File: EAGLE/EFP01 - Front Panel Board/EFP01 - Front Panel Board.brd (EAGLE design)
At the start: 200 x 65 mm, 151 parts, among them J1 PWRBTN, J16 S8B-PH-SM4, J17 S8B-PH-SM4, J18 S6B-PH-SM4, J2 ESTOP, J20 Intel EDISON, J3 USB-A(2.0), J5 LCD, J6 S8B-PH-SM4, J7 USB-B, Q2 25MHz, U1 74LVC1T45, U10 FT231XS-R, U11 74LVC1T45, U12 74LVC1T45, U13 74LVC1T45, U14 74LVC1T45, U15 74LVC1T45, U17 OR, U18 MIC2026-1YM, U19 MIC2026-1YM, U2 74LVC1T45, U20 OR, U21 74LVC1T45, U22 74LVC1T45, U23 74LVC1T45, U24 74LVC1T45, U25 74LVC1T45, U26 74LVC1T45, U27 74LVC1T45, U28 74LVC1T45, U3 93LC66A, U30 74LVC1T45, U4 LAN9514, U5 74LVC1T45, U6 74LVC1T45, U7 74LVC1T45, U8 74LVC1T45, U9 SP3485

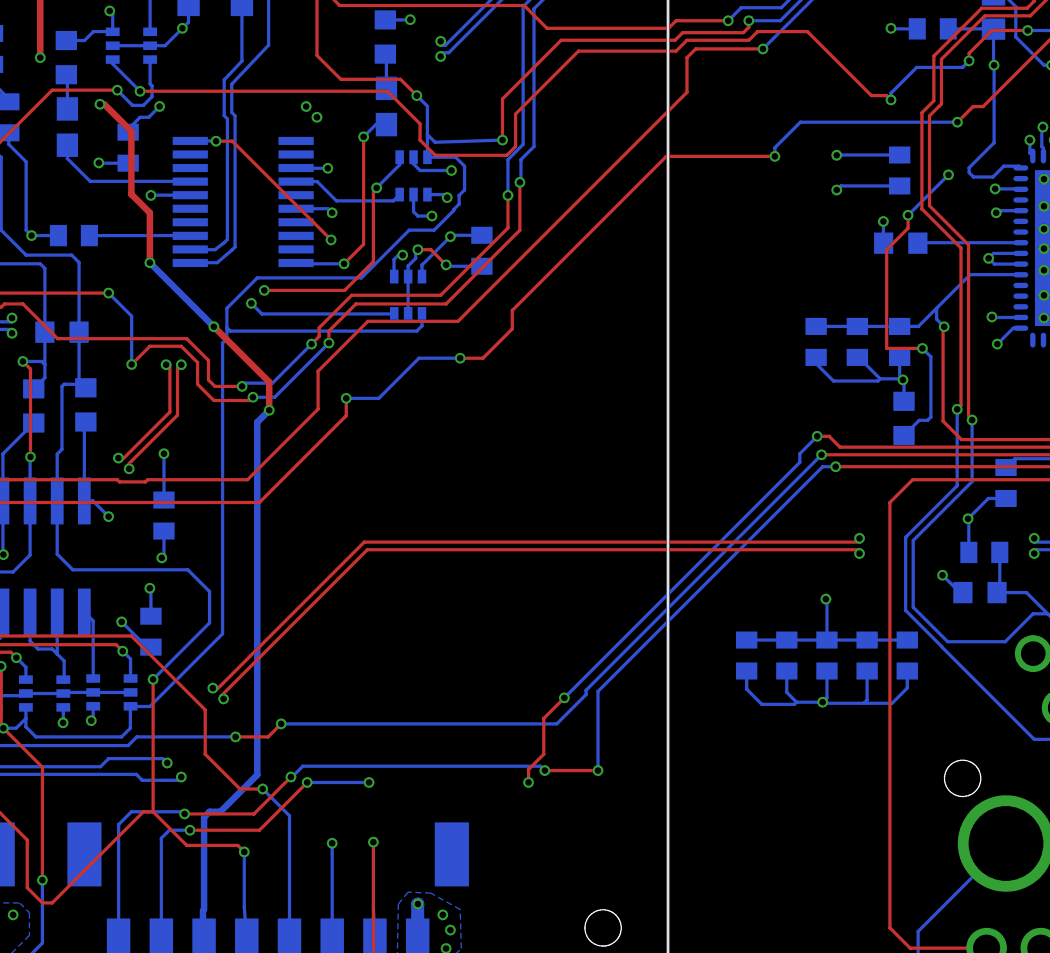
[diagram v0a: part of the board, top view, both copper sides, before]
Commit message: Fixed BOM, began adding DFM changes
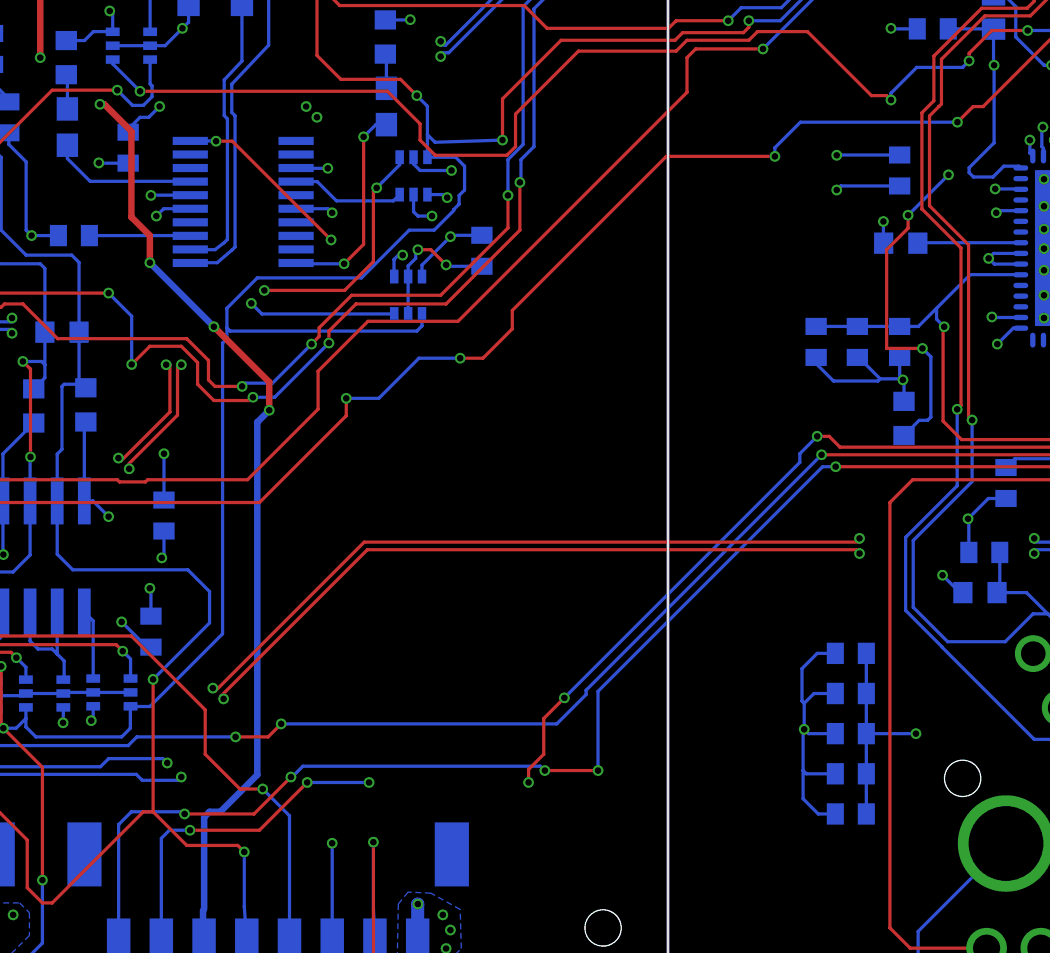
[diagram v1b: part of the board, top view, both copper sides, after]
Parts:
- moved C23 7.87 mm to (154.4, 12.4), turned to 180 degrees
- moved C79 5.59 mm to (154.4, 14.3), turned to 180 degrees
- moved C82 4.88 mm to (154.4, 20.0), turned to 180 degrees
- moved C80 3.82 mm to (154.4, 16.2), turned to 180 degrees
- moved C81 3.48 mm to (154.4, 18.1), turned to 180 degrees
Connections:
- net +3V3: now also U10.15
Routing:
- net +3V3: track 217.1 -> 219.2 mm, vias 60 -> 61

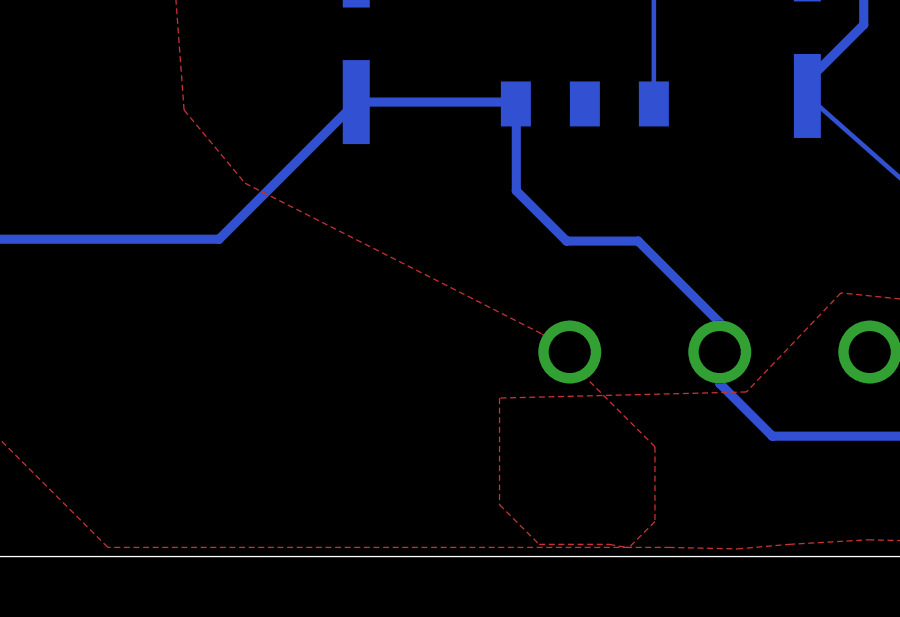
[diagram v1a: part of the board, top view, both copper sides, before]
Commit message: Made REV 2 modifications, including increasing width of power traces, adding vias to power traces, and addition of LEDs to all modular tools. Catch diodes added to ESOL01 board to prevent coils from creating problems "upstream"
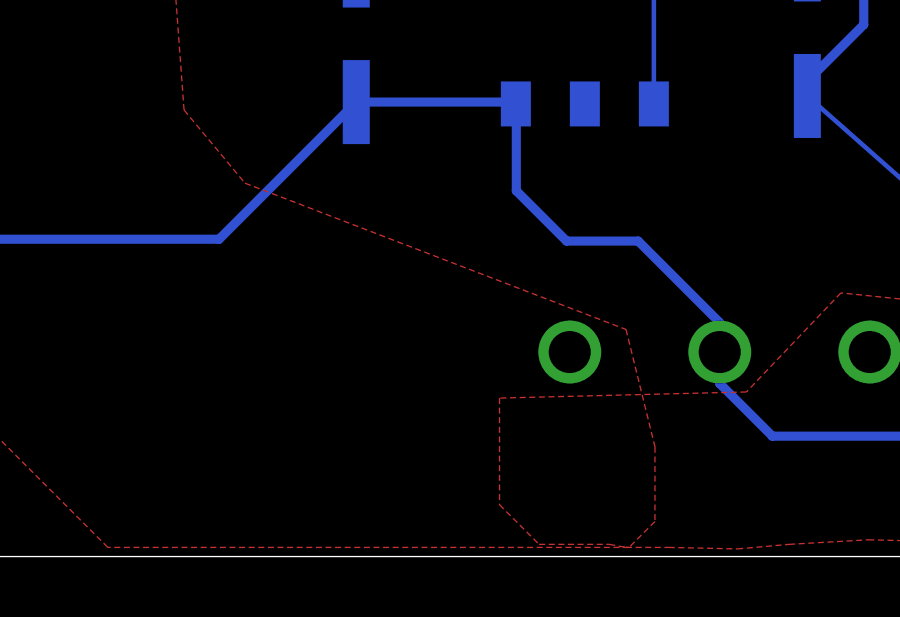
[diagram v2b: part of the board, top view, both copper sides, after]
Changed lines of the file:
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@@
 <polygon width="0" layer="1" thermals="no">
 <vertex x="21.1836" y="12.446"/>
-<vertex x="31.0896" y="7.4168"/>
+<vertex x="33.8836" y="7.5692"/>
 <vertex x="34.8488" y="3.6576"/>
 <vertex x="34.8488" y="1.1684"/>

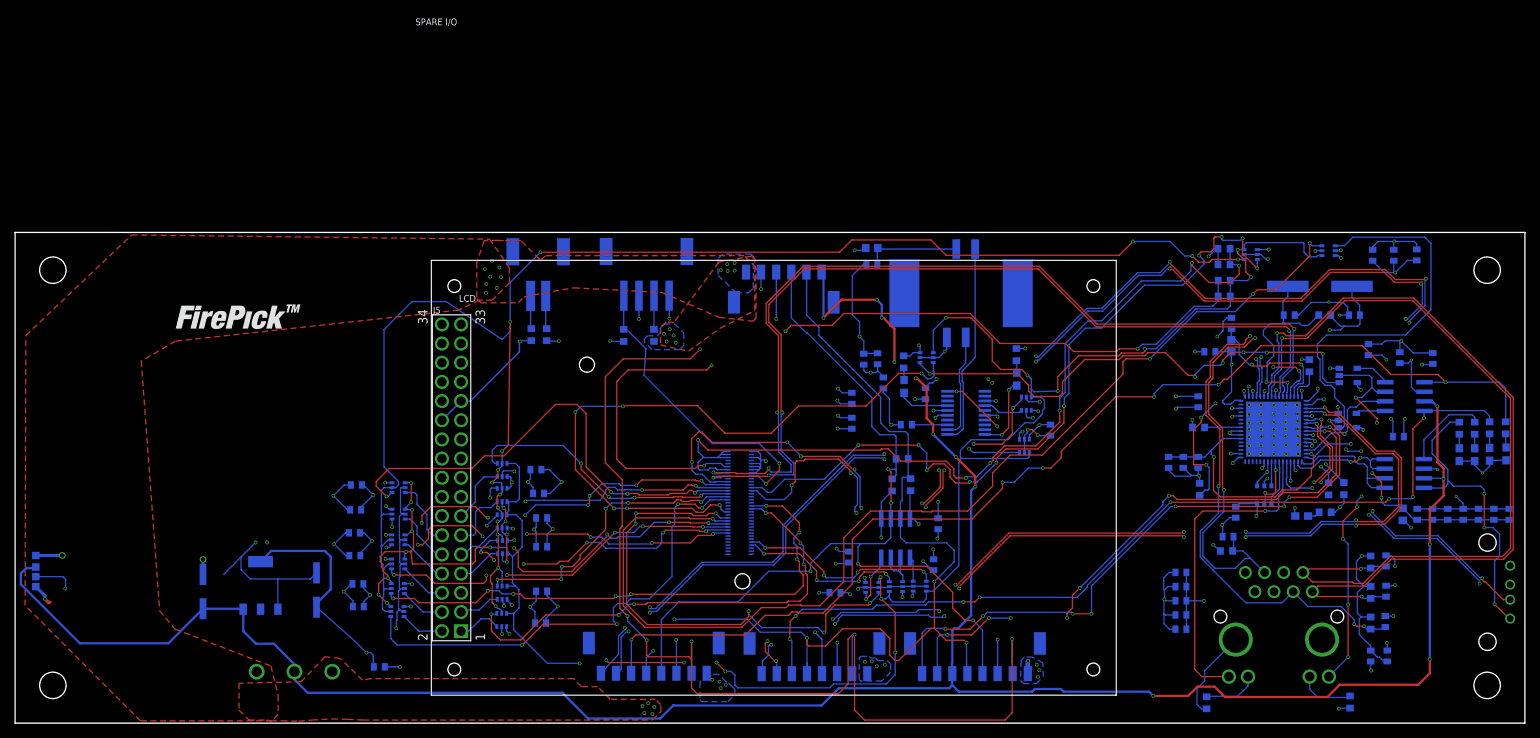
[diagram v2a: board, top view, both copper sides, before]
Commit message: Routing for differential pairs included in EFP01. Minor changes to BOM, inventory list.
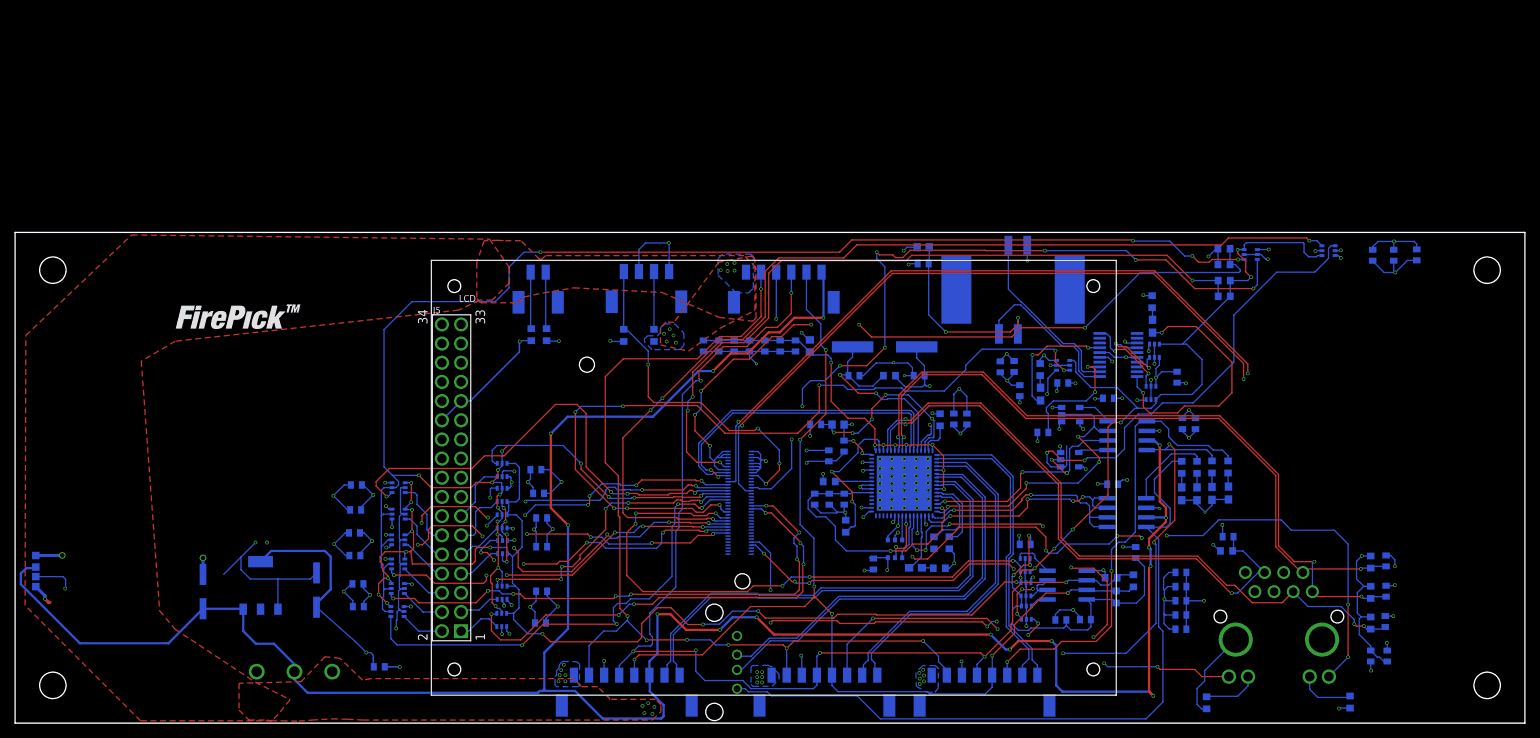
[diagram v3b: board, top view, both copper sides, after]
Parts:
- J1: device TinWhiskers:CON-JST-PH-2.0MM-4P-SMT-RA -> TinWhiskers:CON-JST-PH-2.0MM-4P-SMT-VRT
- J2: device TinWhiskers:CON-JST-PH-2.0MM-2P-SMT-RA -> TinWhiskers:CON-JST-PH-2.0MM-2P-SMT-VRT
- moved C22 109.0 mm to (91.2, 50.0), turned to 90 degrees
- moved C21 105.1 mm to (93.2, 50.0), turned to 90 degrees
- moved J3 102.8 mm to (92.6, 8.05)
- moved C20 101.1 mm to (95.2, 50.0), turned to 90 degrees
- moved C19 97.1 mm to (97.3, 50.0), turned to 90 degrees
- moved C18 93.2 mm to (99.3, 50.0), turned to 90 degrees
- moved C14 89.2 mm to (101.3, 50.0), turned to 90 degrees
- moved C13 85.3 mm to (103.4, 50.0), turned to 90 degrees
- moved FB1 81.6 mm to (105.3, 50.0), turned to 90 degrees
- moved C12 58.2 mm to (119.8, 46.0)
- moved Q2 58.2 mm to (115.2, 49.8)
- moved R11 58.2 mm to (115.8, 46.0)
- moved C11 58.2 mm to (111.1, 46.0)
- moved C73 56.7 mm to (106.0, 39.6), turned to 180 degrees
- moved FB4 53.1 mm to (109.0, 39.5), turned to 180 degrees
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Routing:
- net ULC_N: track 171.6 -> 39.4 mm, vias 9 -> 0
- net ULC_P: track 167.0 -> 38.8 mm, vias 9 -> 0
- net PWR2: track 150.7 -> 61.5 mm, vias 6 -> 2
- net USB0_P: track 122.3 -> 42.9 mm, vias 4 -> 0
- net USB0_N: track 120.8 -> 41.4 mm, vias 4 -> 2
- net EE_N: track 121.0 -> 45.6 mm, vias 8 -> 0
- net EE_P: track 120.4 -> 45.0 mm, vias 9 -> 0
- net PWR3: track 39.8 -> 97.8 mm, vias 3 -> 0
- net ULCENO: track 67.9 -> 10.3 mm, vias 6 -> 2
- net SCED_P: track 53.9 -> 108.7 mm, vias 6 -> 3
- net LED_TXRX: track 39.9 -> 89.7 mm, vias 6 -> 8
- net !ENBL_MOD: track 167.1 -> 124.3 mm
- net N$9: track 37.8 -> 0.00 mm
- net N$4: track 37.8 -> 0.00 mm
- net SCED_N: track 72.5 -> 106.8 mm, vias 9 -> 3
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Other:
- board text removed: "SPARE I/O"

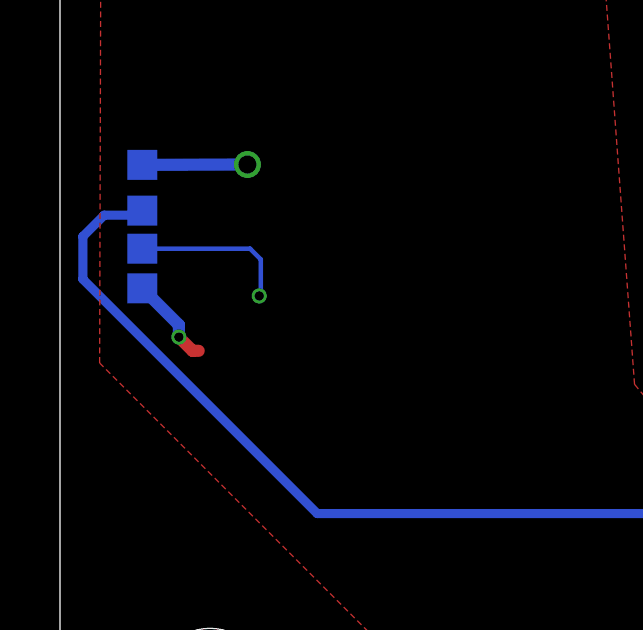
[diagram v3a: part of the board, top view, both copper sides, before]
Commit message: Resistance check, minor changes to EFP01 BOM (100 Ohm changed to 120 Ohm)
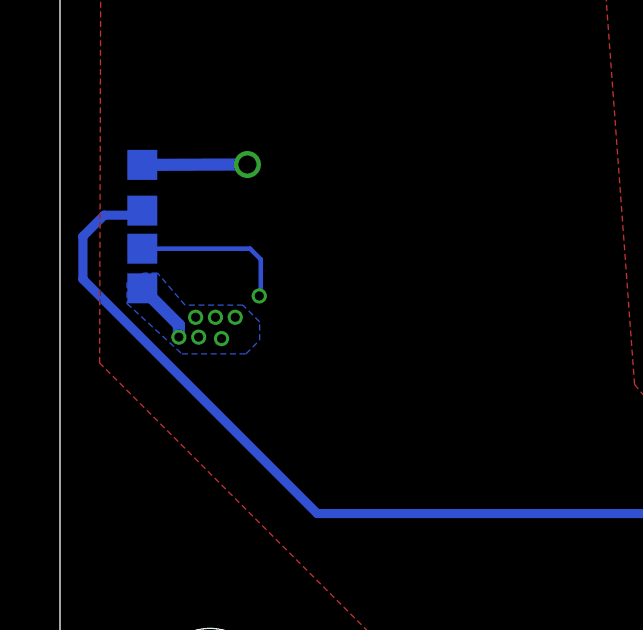
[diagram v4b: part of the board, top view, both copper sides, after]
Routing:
- net +24V: track 2.98 -> 2.13 mm, vias 34 -> 39
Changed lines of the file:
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@@
 <text x="108.0008" y="7.5692" size="0.9" layer="22" font="vector" ratio="12" rot="MR0">END EFFECTOR</text>
 <text x="124.6124" y="7.7216" size="0.9" layer="22" font="vector" ratio="12" rot="MR0">UP-LOOK CAM</text>
-<text x="66.9544" y="60.6044" size="0.9" layer="22" font="vector" ratio="12" rot="MR0">E-STOP</text>
-<text x="82.0928" y="53.1368" size="0.9" layer="22" font="vector" ratio="12" rot="MR0">PWR BTN</text>
-<text x="99.7712" y="52.9336" size="0.9" layer="22" font="vector" ratio="12" rot="MR0">MOD TOOL</text>
+<text x="67.31" y="52.0192" size="0.9" layer="22" font="vector" ratio="12" rot="MR0">E-STOP</text>
+<text x="79.8068" y="52.2224" size="0.9" layer="22" font="vector" ratio="12" rot="MR0">PWR BTN</text>
+<text x="99.7712" y="52.1716" size="0.9" layer="22" font="vector" ratio="12" rot="MR0">MOD TOOL</text>
 <text x="129.2352" y="50.6476" size="0.9" layer="22" font="vector" ratio="12" rot="MR0">USB-B</text>
 <text x="37" y="35" size="0.9" layer="22" ratio="12" rot="MR0">EFP01 Rev --</text>
@@
 <element name="J18" library="TinWhiskers" package="CON-JST-PH-2.00MM-6P-SMT-VRT" value="S6B-PH-SM4" x="101.8286" y="59.7408" smashed="yes" rot="MR180">
 <attribute name="PARTNO" value="B6B-PH-SM4-TB(LF)(SN)" x="101.8286" y="59.7408" size="1.778" layer="28" rot="MR180" display="off"/>
-<attribute name="NAME" x="109.7102" y="53.082" size="0.9" layer="26" font="vector" ratio="12" rot="MR0"/>
+<attribute name="NAME" x="109.4054" y="52.1676" size="0.9" layer="26" font="vector" ratio="12" rot="MR0"/>
 <attribute name="VALUE" x="111.8286" y="54.7408" size="0.9" layer="28" font="vector" ratio="12" rot="MR180"/>
 </element>
@@
 </element>
 <element name="J1" library="TinWhiskers" package="CON-JST-PH-2.0MM-4P-SMT-VRT" value="PWRBTN" x="83.6422" y="59.817" smashed="yes" rot="MR180">
-<attribute name="NAME" x="88.5694" y="53.1462" size="0.9" layer="26" font="vector" ratio="12" rot="MR0"/>
+<attribute name="NAME" x="88.5694" y="52.2826" size="0.9" layer="26" font="vector" ratio="12" rot="MR0"/>
 <attribute name="VALUE" x="91.8722" y="57.547" size="0.9" layer="28" font="vector" ratio="12" rot="MR180"/>
 <attribute name="PARTNO" value="S4B-PH-SM4-TB(LF)(SN)" x="83.6422" y="59.817" size="1.778" layer="28" rot="MR180" display="off"/>
 </element>
 <element name="J2" library="TinWhiskers" package="CON-JST-PH-2.0MM-2P-SMT-VRT" value="ESTOP" x="69.2912" y="59.7408" smashed="yes" rot="MR180">
-<attribute name="NAME" x="72.7196" y="60.4248" size="0.9" layer="26" font="vector" ratio="12" rot="MR0"/>
+<attribute name="NAME" x="72.8212" y="52.1444" size="0.9" layer="26" font="vector" ratio="12" rot="MR0"/>
 <attribute name="VALUE" x="75.9212" y="57.0708" size="0.9" layer="28" font="vector" ratio="12" rot="MR180"/>
 <attribute name="PARTNO" value="S2B-PH-SM4-TB(LF)(SN)" x="69.2912" y="59.7408" size="1.778" layer="28" rot="MR180" display="off"/>
@@
 <wire x1="3.9624" y1="16.8656" x2="3.9624" y2="16.4592" width="0.4064" layer="16"/>
 <via x="3.9624" y="16.4592" extent="1-16" drill="0.3048"/>
-<wire x1="3.9624" y1="16.4592" x2="4.4196" y2="16.002" width="0.4064" layer="1"/>
-<wire x1="4.4196" y1="16.002" x2="4.6228" y2="16.002" width="0.4064" layer="1"/>
 <polygon width="0" layer="1">
 <vertex x="63.9572" y="63.9572"/>
@@
 <via x="119.8372" y="5.1816" extent="1-16" drill="0.3048"/>
 <via x="120.396" y="5.5372" extent="1-16" drill="0.3048"/>
+<polygon width="0.0254" layer="16" thermals="no">
+<vertex x="2.2352" y="18.288"/>
+<vertex x="2.2352" y="17.5768"/>
+<vertex x="4.064" y="15.9004"/>
+<vertex x="6.1976" y="15.9004"/>
+<vertex x="6.6548" y="16.3576"/>
+<vertex x="6.6548" y="16.9672"/>
+<vertex x="6.096" y="17.526"/>
+<vertex x="4.1656" y="17.526"/>
+<vertex x="3.2512" y="18.5928"/>
+<vertex x="2.794" y="18.5928"/>
+</polygon>
+<via x="4.5212" y="17.1196" extent="1-16" drill="0.3048"/>
+<via x="4.6228" y="16.4592" extent="1-16" drill="0.3048"/>
+<via x="5.1816" y="17.1196" extent="1-16" drill="0.3048"/>
+<via x="5.3848" y="16.4084" extent="1-16" drill="0.3048"/>
+<via x="5.842" y="17.1196" extent="1-16" drill="0.3048"/>
 </signal>
 <signal name="N$5">
